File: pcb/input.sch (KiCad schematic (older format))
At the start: 24 parts, among them J4 CONN_01X16, U1 MCP23017, U2 LTV-847, U3 LTV-847, U4 LTV-847, U5 LTV-847

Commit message: Updating PCB
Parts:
- removed C?: 0.1uF, symbol C
- removed C?: 22uF, symbol CP
- removed J4: CONN_01X16, symbol CONN_01X16
- removed R1, R10, R11, R12, R13, R14, R15, R16, R2, R3, R4, R5, R6, R7, R8, R9: 470, symbol R
- removed U1: MCP23017, symbol MCP23017
- removed U2, U3, U4, U5: LTV-847, Housings_DIP:DIP-16_W7.62mm, symbol LTV-847
- added C3: 0.1uF, Capacitor_THT:C_Disc_D5.0mm_W2.5mm_P2.50mm, symbol Device:C
- added J10, J9: Screw_Terminal_01x08, TerminalBlock_TE-Connectivity:TerminalBlock_TE_282834-8_1x08_P2.54mm_Horizontal, symbol Connector:Screw_Terminal_01x08
- added U2: MCP23017-E_SP, Package_DIP:DIP-28_W7.62mm, symbol dk_Interface-I-O-Expanders:MCP23017-E_SP
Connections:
- net labels added: Pin0, Pin1, Pin10, Pin11, Pin12, Pin13, Pin14, Pin15, Pin2, Pin3, Pin4, Pin5, Pin6, Pin7, Pin8, Pin9, ~RESET
- net labels removed: GNDD, GPA0, GPA1, GPA2, GPA3, GPA4, GPA5, GPA6, GPA7, GPA[0..3], GPA[0..7], GPA[4..7], GPB0, GPB1, GPB2, GPB3, GPB4, GPB5, GPB6, GPB7, GPB[0..3], GPB[0..7], GPB[4..7], IN[0..15], IN[0..3], IN[0..7], IN[12..15], IN[4..7], IN[8..11], IN[8..15], RESET
- wire segments 126 -> 78

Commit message: latest
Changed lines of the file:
@@
 AR Path="/5C211542/5C211768" Ref="U2"  Part="1"
 AR Path="/5C211551/5C211768" Ref="U7"  Part="1"
-F 0 "U2" H 3850 2600 60  0000 C CNN
+F 0 "U7" H 3850 2600 60  0000 C CNN
 F 1 "MCP23017-E_SP" H 3850 2494 60  0000 C CNN
 F 2 "Package_DIP:DIP-28_W7.62mm" H 3950 1800 60  0001 L CNN
@@
 AR Path="/5C211542/5C211A11" Ref="#PWR025"  Part="1"
 AR Path="/5C211551/5C211A11" Ref="#PWR036"  Part="1"
-F 0 "#PWR025" H 4450 600 50  0001 C CNN
+F 0 "#PWR036" H 4450 600 50  0001 C CNN
 F 1 "+5V" H 4465 923 50  0000 C CNN
 F 2 "" H 4450 750 50  0001 C CNN
@@
 AR Path="/5C211542/5C2127BA" Ref="#PWR024"  Part="1"
 AR Path="/5C211551/5C2127BA" Ref="#PWR035"  Part="1"
-F 0 "#PWR024" H 3850 3000 50  0001 C CNN
+F 0 "#PWR035" H 3850 3000 50  0001 C CNN
 F 1 "GND" V 3855 3122 50  0000 R CNN
 F 2 "" H 3850 3250 50  0001 C CNN
@@
 AR Path="/5C211542/5C2C6D1A" Ref="C3"  Part="1"
 AR Path="/5C211551/5C2C6D1A" Ref="C4"  Part="1"
-F 0 "C3" H 5115 1046 50  0000 L CNN
+F 0 "C4" H 5115 1046 50  0000 L CNN
 F 1 "0.1uF" H 5115 955 50  0000 L CNN
 F 2 "Capacitor_THT:C_Disc_D5.0mm_W2.5mm_P2.50mm" H 5038 850 50  0001 C CNN
@@
 AR Path="/5C211542/5C2C6D8B" Ref="#PWR026"  Part="1"
 AR Path="/5C211551/5C2C6D8B" Ref="#PWR037"  Part="1"
-F 0 "#PWR026" H 5000 1000 50  0001 C CNN
+F 0 "#PWR037" H 5000 1000 50  0001 C CNN
 F 1 "GND" H 5005 1077 50  0000 C CNN
 F 2 "" H 5000 1250 50  0001 C CNN
@@
 AR Path="/5C211551/5C2B8202" Ref="J9"  Part="1"
 AR Path="/5C211542/5C2B8202" Ref="J7"  Part="1"
-F 0 "J7" H 4020 6517 50  0000 C CNN
+F 0 "J9" H 4020 6517 50  0000 C CNN
 F 1 "Screw_Terminal_01x08" H 4020 6426 50  0000 C CNN
 F 2 "TerminalBlock_TE-Connectivity:TerminalBlock_TE_282834-8_1x08_P2.54mm_Horizontal" H 4100 6000 50  0001 C CNN
@@
 AR Path="/5C211551/5C2BD2C4" Ref="J10"  Part="1"
 AR Path="/5C211542/5C2BD2C4" Ref="J8"  Part="1"
-F 0 "J8" H 8970 6517 50  0000 C CNN
+F 0 "J10" H 8970 6517 50  0000 C CNN
 F 1 "Screw_Terminal_01x08" H 8970 6426 50  0000 C CNN
 F 2 "TerminalBlock_TE-Connectivity:TerminalBlock_TE_282834-8_1x08_P2.54mm_Horizontal" H 9050 6000 50  0001 C CNN

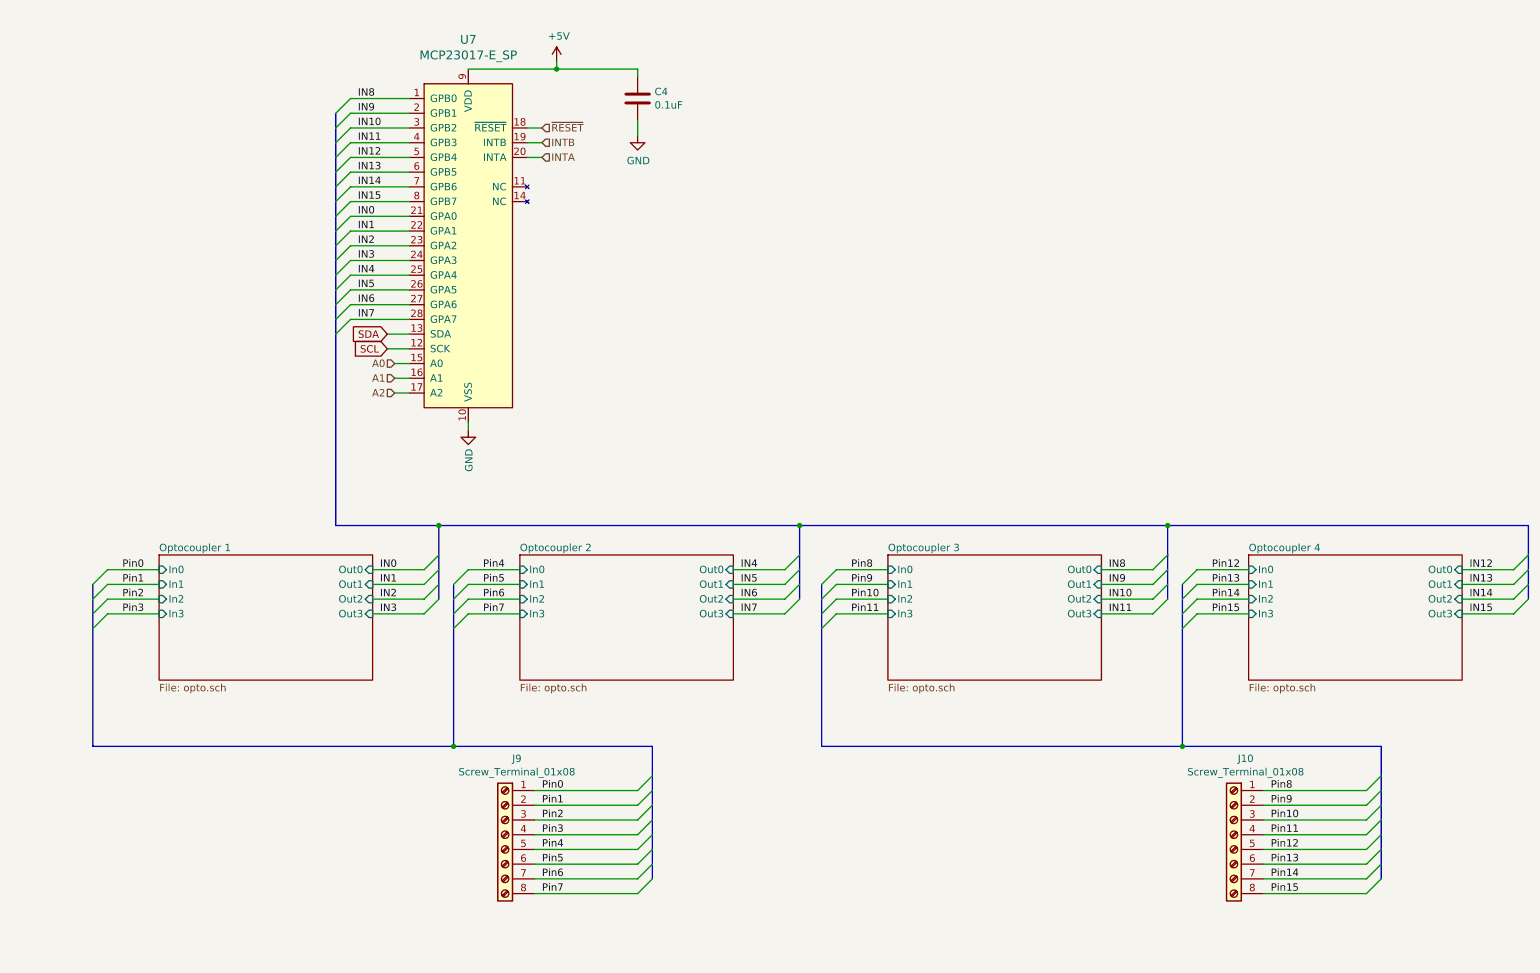
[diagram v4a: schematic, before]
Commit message: Changed some footprints, spacing out components
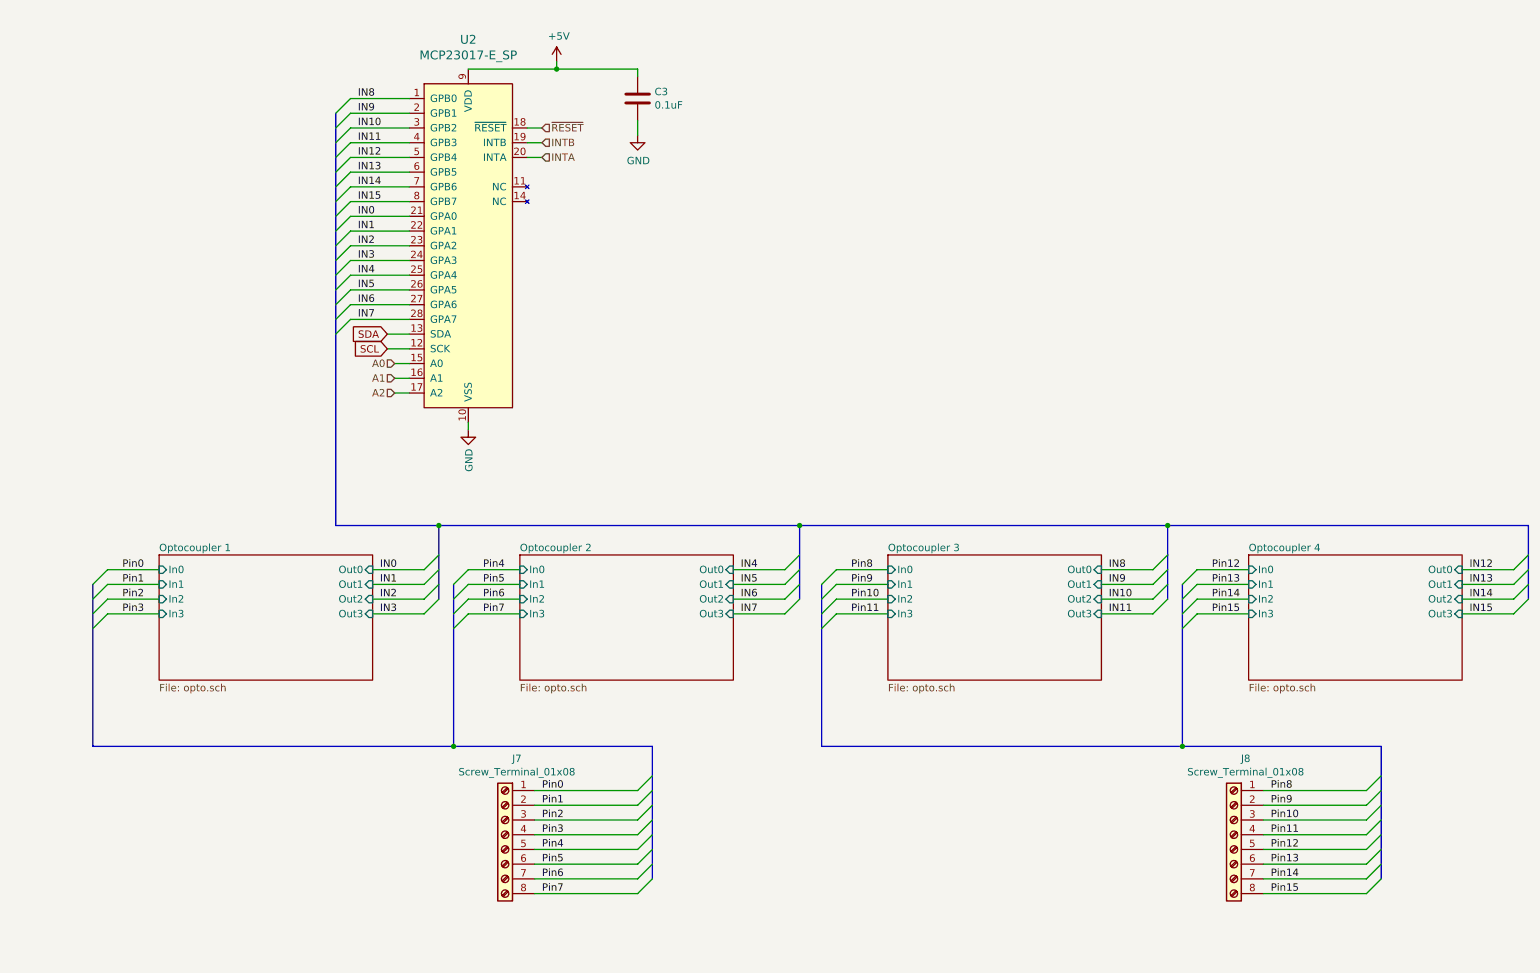
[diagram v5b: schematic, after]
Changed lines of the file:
@@
 $Descr A4 11693 8268
 encoding utf-8
-Sheet 7 45
+Sheet 2 45
 Title "Standaert Home Automation"
 Date ""
@@
 AR Path="/5C211542/5C211768" Ref="U2"  Part="1"
 AR Path="/5C211551/5C211768" Ref="U7"  Part="1"
-F 0 "U7" H 3850 2600 60  0000 C CNN
+F 0 "U2" H 3850 2600 60  0000 C CNN
 F 1 "MCP23017-E_SP" H 3850 2494 60  0000 C CNN
 F 2 "Package_DIP:DIP-28_W7.62mm" H 3950 1800 60  0001 L CNN
@@
 AR Path="/5C211542/5C2C6D1A" Ref="C3"  Part="1"
 AR Path="/5C211551/5C2C6D1A" Ref="C4"  Part="1"
-F 0 "C4" H 5115 1046 50  0000 L CNN
+F 0 "C3" H 5115 1046 50  0000 L CNN
 F 1 "0.1uF" H 5115 955 50  0000 L CNN
 F 2 "Capacitor_THT:C_Disc_D5.0mm_W2.5mm_P2.50mm" H 5038 850 50  0001 C CNN
@@
 AR Path="/5C211551/5C2B8202" Ref="J9"  Part="1"
 AR Path="/5C211542/5C2B8202" Ref="J7"  Part="1"
-F 0 "J9" H 4020 6517 50  0000 C CNN
+F 0 "J7" H 4020 6517 50  0000 C CNN
 F 1 "Screw_Terminal_01x08" H 4020 6426 50  0000 C CNN
 F 2 "TerminalBlock_TE-Connectivity:TerminalBlock_TE_282834-8_1x08_P2.54mm_Horizontal" H 4100 6000 50  0001 C CNN
@@
 AR Path="/5C211551/5C2BD2C4" Ref="J10"  Part="1"
 AR Path="/5C211542/5C2BD2C4" Ref="J8"  Part="1"
-F 0 "J10" H 8970 6517 50  0000 C CNN
+F 0 "J8" H 8970 6517 50  0000 C CNN
 F 1 "Screw_Terminal_01x08" H 8970 6426 50  0000 C CNN
 F 2 "TerminalBlock_TE-Connectivity:TerminalBlock_TE_282834-8_1x08_P2.54mm_Horizontal" H 9050 6000 50  0001 C CNN
